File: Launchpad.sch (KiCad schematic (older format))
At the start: 24 parts, among them J18 Screw_Terminal_01x02, Q1 BSS138, SW3 SW_SPDT, U10 msp-exp430f5529-LP, U11 MCP73831, U12 TPS73733

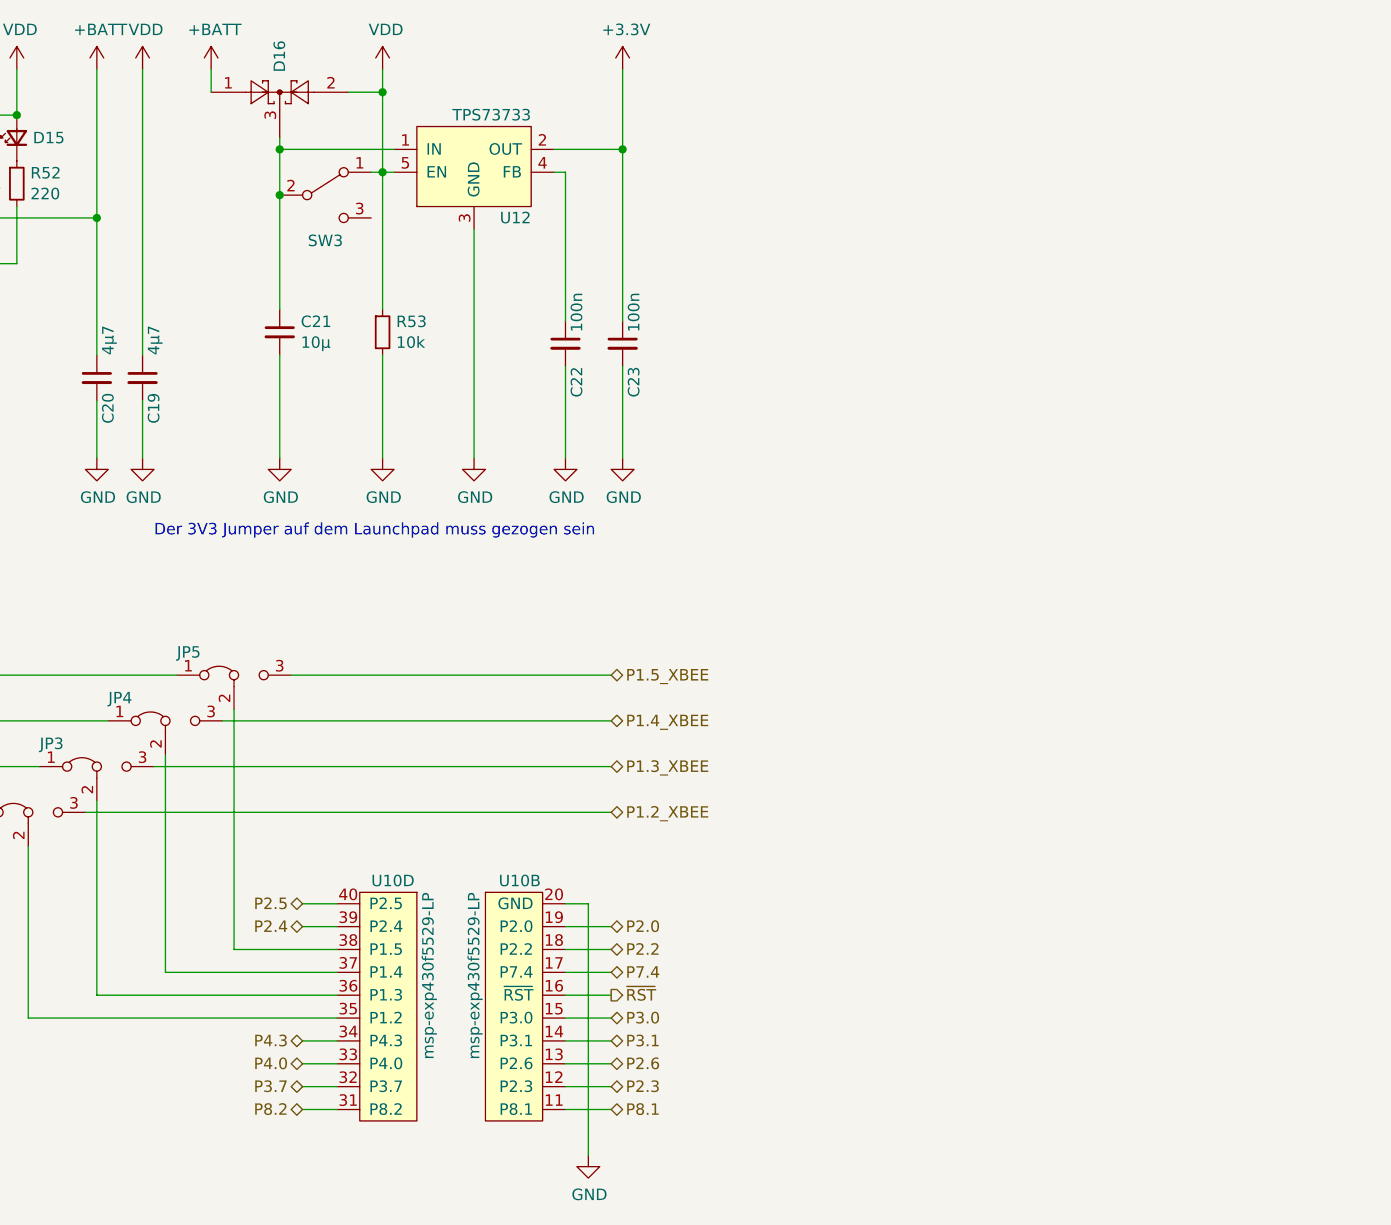
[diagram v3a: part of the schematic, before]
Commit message: Anpassungen am Lüfteranschluss und den LEDs
-Lüfteranschluss verändert
 -> 12V-Versorgung eingefügt
-LED & LCD auf 3,3V umgestellt
 -> Ladungspunpe für neg. Kontrastspannung
-keine 5V Versorgung mehr
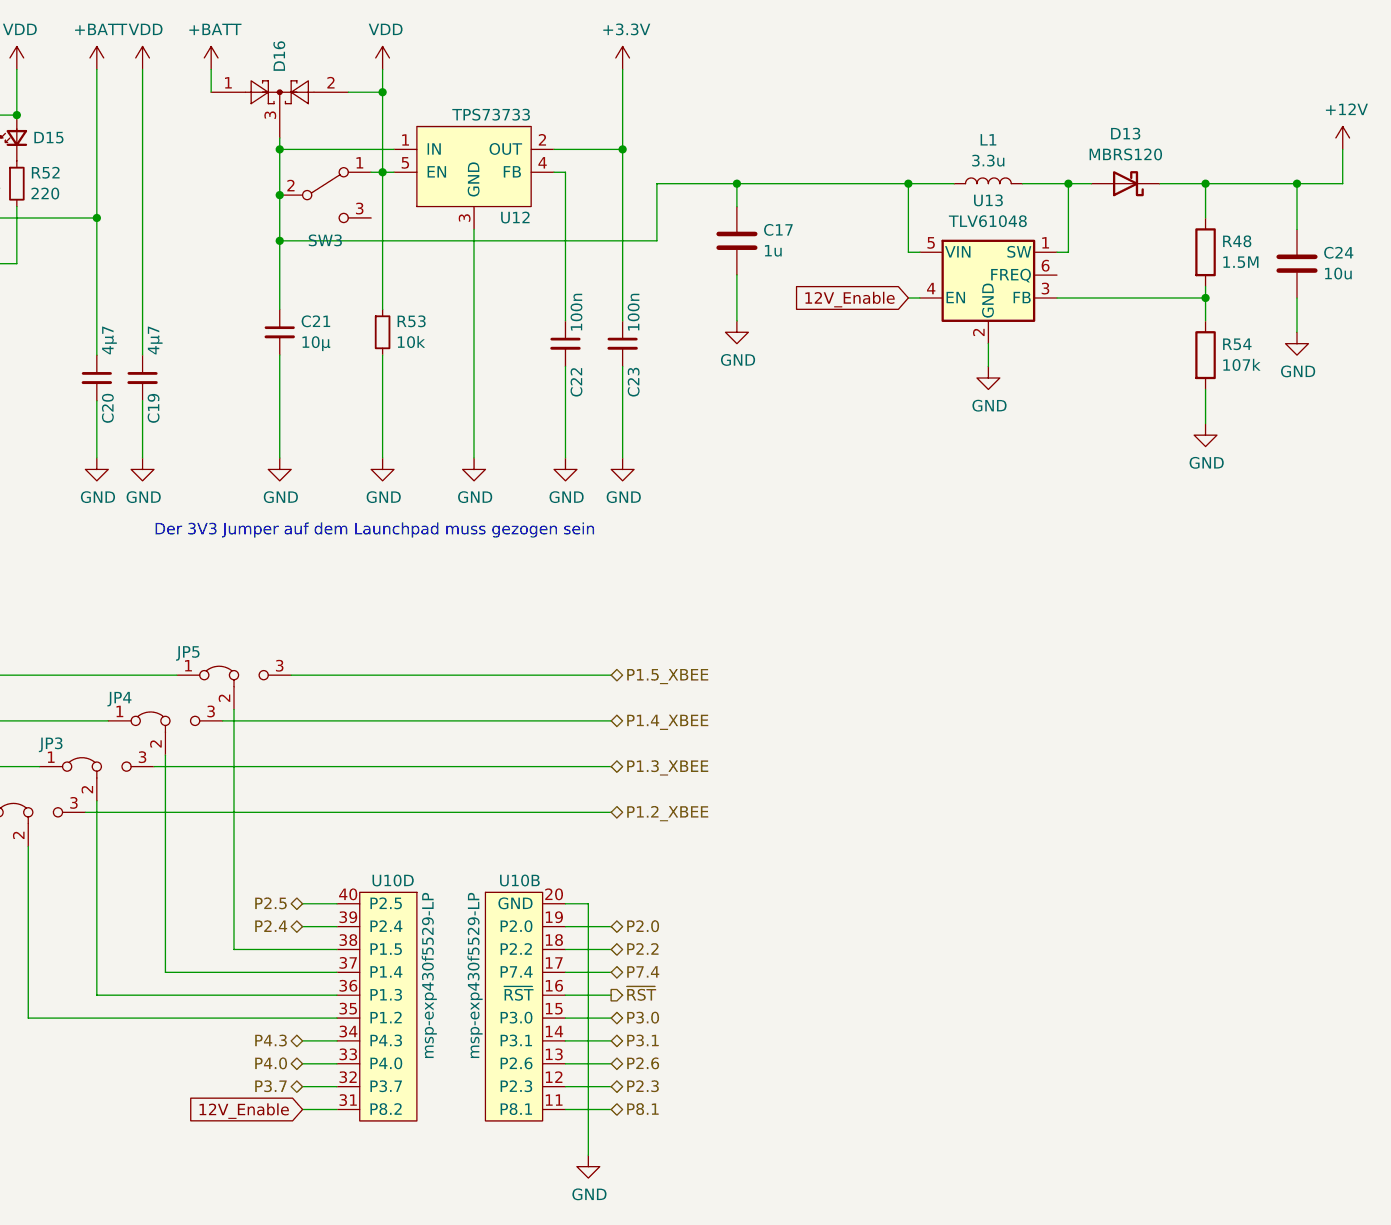
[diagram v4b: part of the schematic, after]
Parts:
- added C17: 1u, Capacitor_SMD:C_0603_1608Metric_Pad1.05x0.95mm_HandSolder, symbol Device:C
- added C24: 10u, Capacitor_SMD:C_1206_3216Metric_Pad1.42x1.75mm_HandSolder, symbol Device:C
- added D13: MBRS120, Diode_SMD:D_SMB_Handsoldering, symbol HS-Wismar:MBRS120
- added L1: 3.3u, HS-Wismar:L_Coilcraft_XxL4040_handsolder, symbol Device:L
- added R48: 1.5M, Resistor_SMD:R_0603_1608Metric_Pad1.05x0.95mm_HandSolder, symbol Device:R
- added R54: 107k, Resistor_SMD:R_0603_1608Metric_Pad1.05x0.95mm_HandSolder, symbol Device:R
- added U13: TLV61048, Package_TO_SOT_SMD:SOT-23-6, symbol HS-Wismar:TLV61048
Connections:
- net GND: now also C17.2, C24.2, R54.2, U13.2 (GND)
- net at C21.1, D16.3, SW3.2 (B)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: now also C17.1, L1.1, U13.5 (VIN)
- net P8.2 renamed 12V_Enable
- net 12V_Enable: now also U13.4 (EN)
- new net: R48.2, R54.1, U13.3 (FB)
- new net: D13.2 (A), L1.2, U13.1 (SW)
- new net +12V: C24.1, D13.1 (K), R48.1
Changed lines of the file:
@@
 Text HLabel 6450 5800 0    50   BiDi ~ 0
 P3.7
-Text HLabel 6450 5900 0    50   BiDi ~ 0
-P8.2
 Text HLabel 4400 5200 2    50   BiDi ~ 0
 P6.0
@@
 Wire Wire Line
 	6800 3050 6800 2600
-Wire Wire Line
-	6800 2400 6800 1800
 $Comp
 L MCT_Labor_5529-rescue:SW_SPDT-Switch SW3
@@
 Connection ~ 6350 1900
 Wire Wire Line
-	6350 1900 6350 2400
-Wire Wire Line
 	6750 1800 6800 1800
 $Comp
@@
 	1    0    0    -1
 $EndComp
+$Comp
+L Device:R R48
+U 1 1 5F20D2E2
+P 10400 2150
+F 0 "R48" H 10470 2196 50  0000 L CNN
+F 1 "1.5M" H 10470 2105 50  0000 L CNN
+F 2 "Resistor_SMD:R_0603_1608Metric_Pad1.05x0.95mm_HandSolder" V 10330 2150 50  0001 C CNN
+F 3 "~" H 10400 2150 50  0001 C CNN
+	1    10400 2150
+	1    0    0    -1
+$EndComp
+$Comp
+L Device:R R54
+U 1 1 5F20DD13
+P 10400 2600
+F 0 "R54" H 10470 2646 50  0000 L CNN
+F 1 "107k" H 10470 2555 50  0000 L CNN
+F 2 "Resistor_SMD:R_0603_1608Metric_Pad1.05x0.95mm_HandSolder" V 10330 2600 50  0001 C CNN
+F 3 "~" H 10400 2600 50  0001 C CNN
+	1    10400 2600
+	1    0    0    -1
+$EndComp
+$Comp
+L Device:C C24
+U 1 1 5F20ECDB
+P 10800 2200
+F 0 "C24" H 10915 2246 50  0000 L CNN
+F 1 "10u" H 10915 2155 50  0000 L CNN
+F 2 "Capacitor_SMD:C_1206_3216Metric_Pad1.42x1.75mm_HandSolder" H 10838 2050 50  0001 C CNN
+F 3 "~" H 10800 2200 50  0001 C CNN
+	1    10800 2200
+	1    0    0    -1
+$EndComp
+$Comp
+L Device:L L1
+U 1 1 5F20FFC5
+P 9450 1850
+F 0 "L1" V 9640 1850 50  0000 C CNN
+F 1 "3.3u" V 9549 1850 50  0000 C CNN
+F 2 "HS-Wismar:L_Coilcraft_XxL4040_handsolder" H 9450 1850 50  0001 C CNN
+F 3 "~" H 9450 1850 50  0001 C CNN
+	1    9450 1850
+	0    -1   -1   0
+$EndComp
+$Comp
+L HS-Wismar:MBRS120 D13
+U 1 1 5F22189B
+P 10050 1850
+F 0 "D13" H 10050 1633 50  0000 C CNN
+F 1 "MBRS120" H 10050 1724 50  0000 C CNN
+F 2 "Diode_SMD:D_SMB_Handsoldering" H 10050 1675 50  0001 C CNN
+F 3 "https://www.mouser.de/datasheet/2/308/MBRS120T3-D-1381807.pdf" H 10050 1850 50  0001 C CNN
+	1    10050 1850
+	-1   0    0    1
+$EndComp
+Wire Wire Line
+	9600 1850 9800 1850
+Wire Wire Line
+	9750 2150 9800 2150
+Wire Wire Line
+	9800 2150 9800 1850
+Connection ~ 9800 1850
+Wire Wire Line
+	9800 1850 9900 1850
+Wire Wire Line
+	10200 1850 10400 1850
+Wire Wire Line
+	11000 1850 11000 1700
+Connection ~ 10800 1850
+Wire Wire Line
+	10800 1850 11000 1850
+Wire Wire Line
+	10800 1850 10800 2050
+$Comp
+L power:GND #PWR05
+U 1 1 5F2393ED
+P 10800 2500
+F 0 "#PWR05" H 10800 2250 50  0001 C CNN
+F 1 "GND" H 10805 2327 50  0000 C CNN
+F 2 "" H 10800 2500 50  0001 C CNN
+F 3 "" H 10800 2500 50  0001 C CNN
+	1    10800 2500
+	1    0    0    -1
+$EndComp
+$Comp
+L power:GND #PWR04
+U 1 1 5F239D9A
+P 10400 2900
+F 0 "#PWR04" H 10400 2650 50  0001 C CNN
+F 1 "GND" H 10405 2727 50  0000 C CNN
+F 2 "" H 10400 2900 50  0001 C CNN
+F 3 "" H 10400 2900 50  0001 C CNN
+	1    10400 2900
+	1    0    0    -1
+$EndComp
+$Comp
+L power:GND #PWR03
+U 1 1 5F23AC8B
+P 9450 2650
+F 0 "#PWR03" H 9450 2400 50  0001 C CNN
+F 1 "GND" H 9455 2477 50  0000 C CNN
+F 2 "" H 9450 2650 50  0001 C CNN
+F 3 "" H 9450 2650 50  0001 C CNN
+	1    9450 2650
+	1    0    0    -1
+$EndComp
+$Comp
+L power:GND #PWR02
+U 1 1 5F23B02B
+P 8350 2450
+F 0 "#PWR02" H 8350 2200 50  0001 C CNN
+F 1 "GND" H 8355 2277 50  0000 C CNN
+F 2 "" H 8350 2450 50  0001 C CNN
+F 3 "" H 8350 2450 50  0001 C CNN
+	1    8350 2450
+	1    0    0    -1
+$EndComp
+Wire Wire Line
+	10800 2350 10800 2500
+Wire Wire Line
+	10400 2000 10400 1850
+Connection ~ 10400 1850
+Wire Wire Line
+	10400 1850 10800 1850
+Wire Wire Line
+	10400 2450 10400 2350
+Wire Wire Line
+	10400 2750 10400 2900
+Wire Wire Line
+	9750 2350 10400 2350
+Connection ~ 10400 2350
+Wire Wire Line
+	10400 2350 10400 2300
+Wire Wire Line
+	9300 1850 9100 1850
+Wire Wire Line
+	9150 2150 9100 2150
+Wire Wire Line
+	9100 2150 9100 1850
+Connection ~ 9100 1850
+Wire Wire Line
+	9450 2550 9450 2650
+$Comp
+L power:+12V #PWR06
+U 1 1 5F26FEA2
+P 11000 1700
+F 0 "#PWR06" H 11000 1550 50  0001 C CNN
+F 1 "+12V" H 11015 1873 50  0000 C CNN
+F 2 "" H 11000 1700 50  0001 C CNN
+F 3 "" H 11000 1700 50  0001 C CNN
+	1    11000 1700
+	1    0    0    -1
+$EndComp
+$Comp
+L HS-Wismar:TLV61048 U13
+U 1 1 5F223F5E
+P 9450 2350
+F 0 "U13" H 9450 2775 50  0000 C CNN
+F 1 "TLV61048" H 9450 2684 50  0000 C CNN
+F 2 "Package_TO_SOT_SMD:SOT-23-6" H 9500 2200 50  0001 L CIN
+F 3 "http://www.ti.com/lit/ds/symlink/tlv61046a.pdf" H 9450 2450 50  0001 C CNN
+	1    9450 2350
+	1    0    0    -1
+$EndComp
+$Comp
+L Device:C C17
+U 1 1 5F20F661
+P 8350 2100
+F 0 "C17" H 8465 2146 50  0000 L CNN
+F 1 "1u" H 8465 2055 50  0000 L CNN
+F 2 "Capacitor_SMD:C_0603_1608Metric_Pad1.05x0.95mm_HandSolder" H 8388 1950 50  0001 C CNN
+F 3 "~" H 8350 2100 50  0001 C CNN
+	1    8350 2100
+	1    0    0    -1
+$EndComp
+Wire Wire Line
+	6800 1800 6800 2400
+Text GLabel 9100 2350 0    50   Input ~ 0
+12V_Enable
+Wire Wire Line
+	6350 1900 6350 2100
+Wire Wire Line
+	8000 1850 8000 2100
+Wire Wire Line
+	8000 2100 6350 2100
+Connection ~ 6350 2100
+Wire Wire Line
+	6350 2100 6350 2400
+Wire Wire Line
+	8000 1850 8350 1850
+Wire Wire Line
+	8350 1850 8350 1950
+Connection ~ 8350 1850
+Wire Wire Line
+	8350 1850 9100 1850
+Wire Wire Line
+	8350 2250 8350 2450
+Wire Wire Line
+	9100 2350 9150 2350
+Text GLabel 6450 5900 0    50   Input ~ 0
+12V_Enable
 $EndSCHEMATC

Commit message: Erster vorab Release - Fertigungsdaten erstellt
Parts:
- D13: symbol HS-Wismar:MBRS120 -> MCT_Labor_5529-rescue:MBRS120-HS-Wismar
- U13: symbol HS-Wismar:TLV61048 -> MCT_Labor_5529-rescue:TLV61048-HS-Wismar
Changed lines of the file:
@@
 $EndComp
 $Comp
-L HS-Wismar:MBRS120 D13
+L MCT_Labor_5529-rescue:MBRS120-HS-Wismar D13
 U 1 1 5F22189B
 P 10050 1850
+AR Path="/5F22189B" Ref="D13"  Part="1"
+AR Path="/5F0B42CA/5F22189B" Ref="D13"  Part="1"
 F 0 "D13" H 10050 1633 50  0000 C CNN
 F 1 "MBRS120" H 10050 1724 50  0000 C CNN
@@
 $EndComp
 $Comp
-L HS-Wismar:TLV61048 U13
+L MCT_Labor_5529-rescue:TLV61048-HS-Wismar U13
 U 1 1 5F223F5E
 P 9450 2350
